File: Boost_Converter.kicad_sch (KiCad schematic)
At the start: 19 parts, among them U3 XL6019E1, U6 MCP4161-502E/SN

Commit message: inital layout
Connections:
- net Boost_In: no longer R18.2, R21.1, TP6.1, U6.5 (P0A)
- net GND: now also R18.2, R21.1, TP6.1, U6.5 (P0A)
- net SW_NODE: now reaches D2.2, L1.2, U3.3 (SW), U3.6 (SW)
- net Feeback: now reaches R14.2, R16.1, U3.5 (FB)
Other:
- moved on the sheet: R16, R21, R27, R28

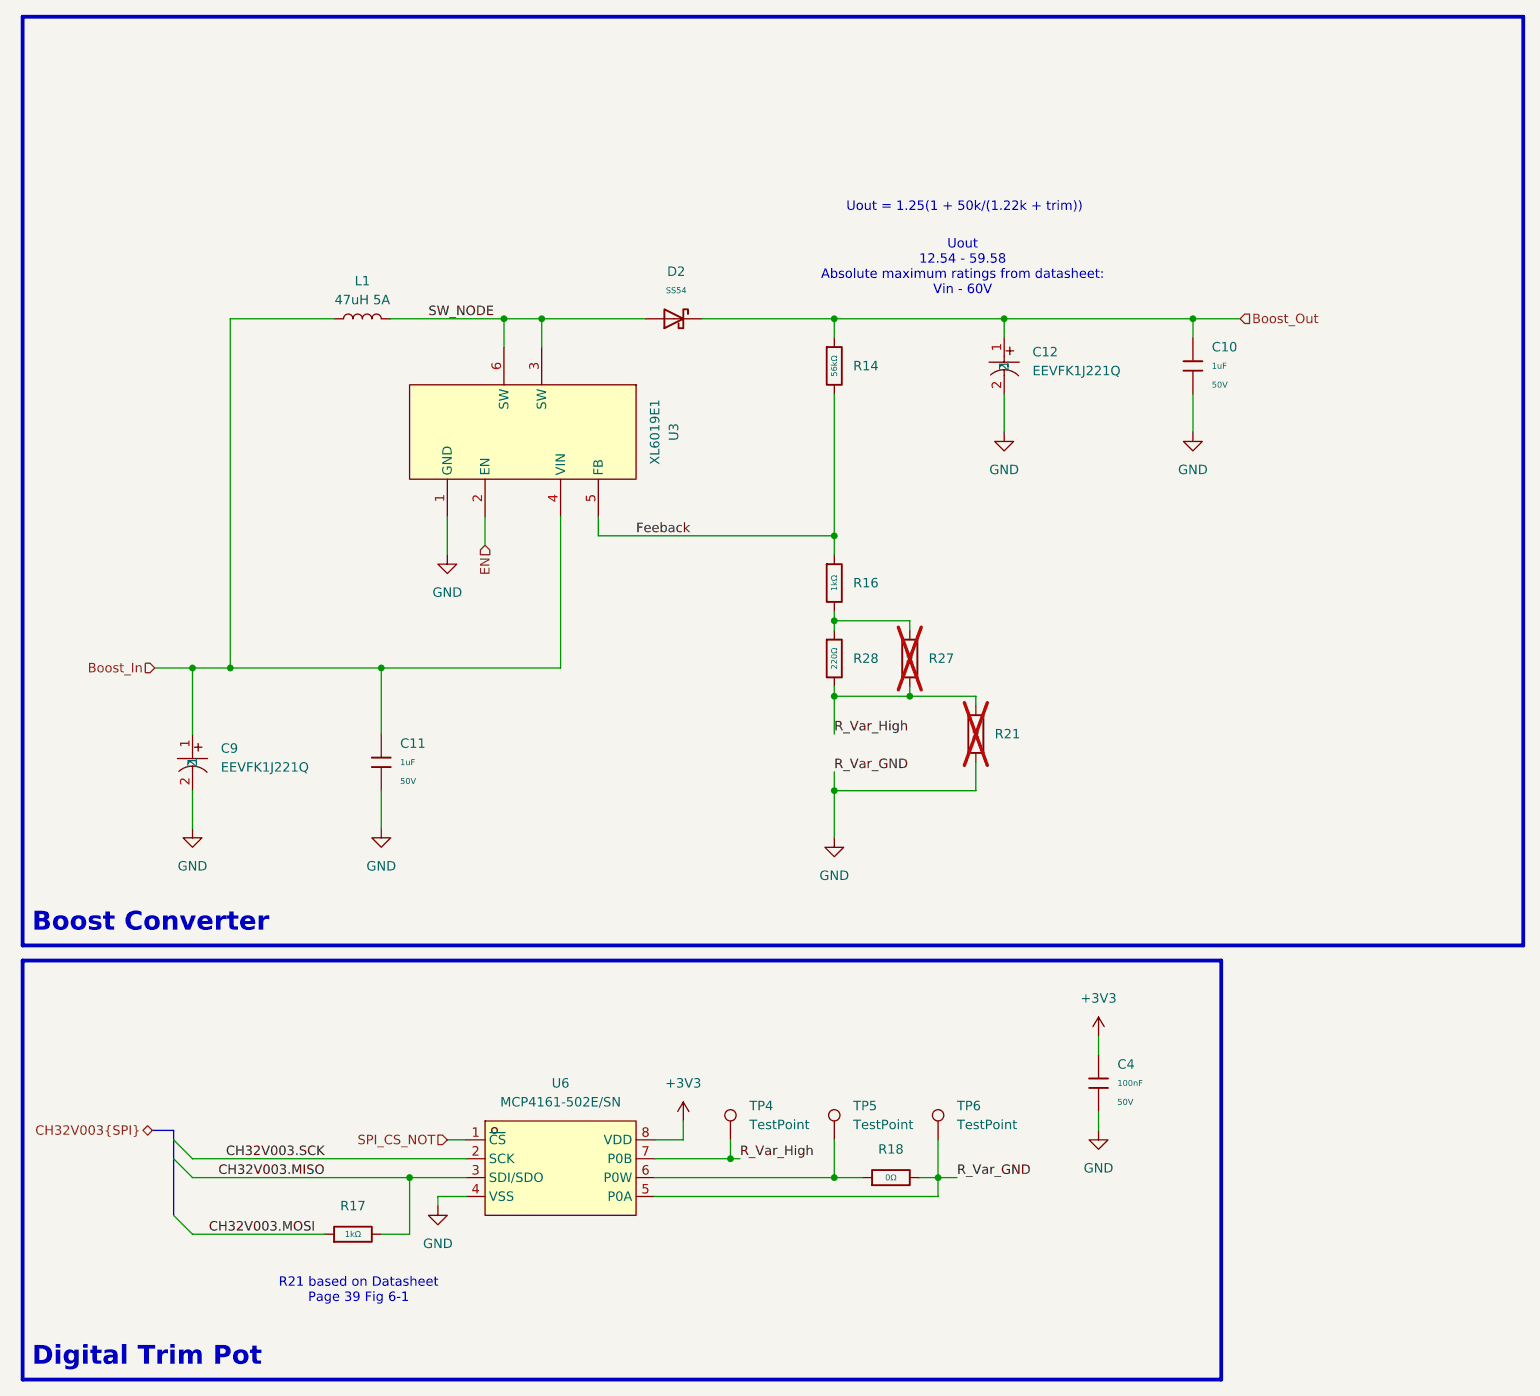
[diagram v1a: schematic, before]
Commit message: commit before removing all the diodes :"
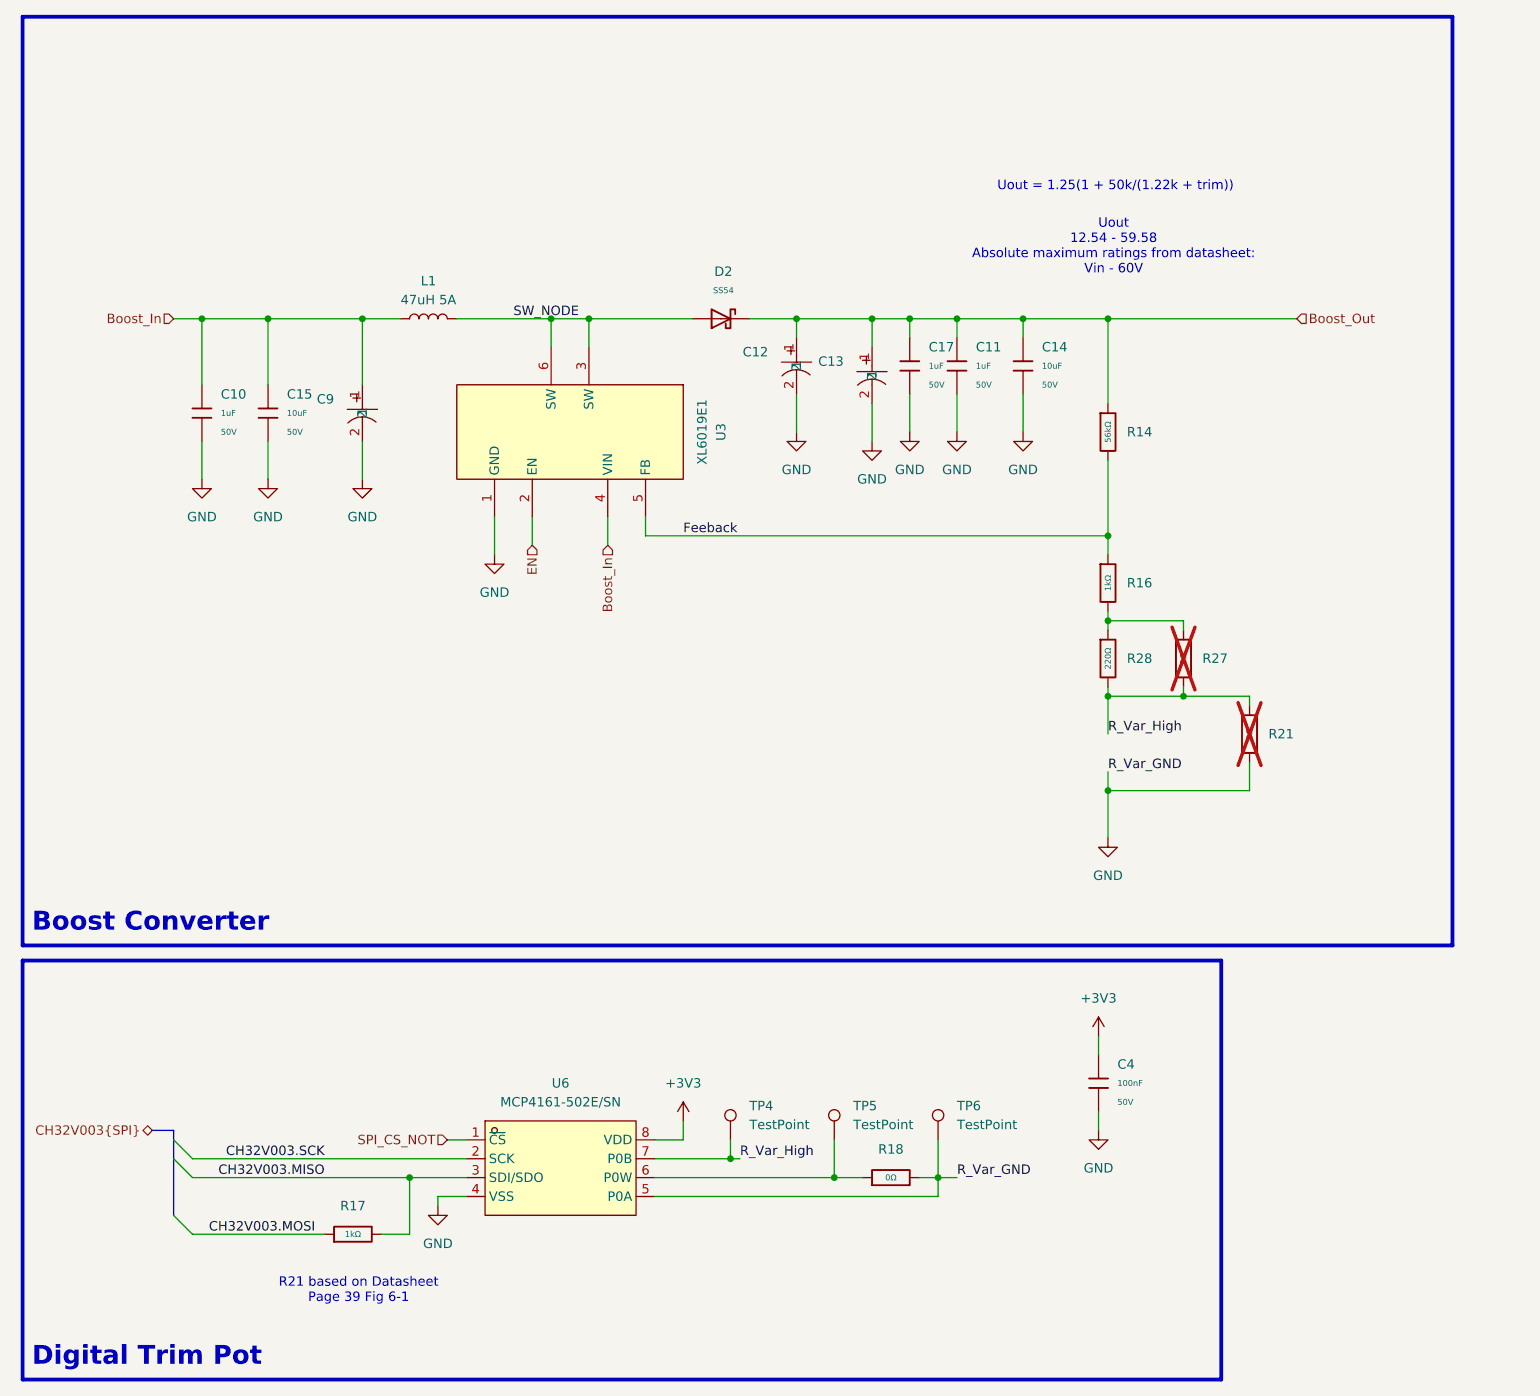
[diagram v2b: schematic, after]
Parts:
- added C13: Whatever the chinese man has (preferably 220uF), Capacitor_SMD:CP_Elec_10x10, symbol EEVFK1J221Q:EEVFK1J221Q
- added C14, C15: 10uF, PCM_JLCPCB:C_1206, symbol PCM_JLCPCB-Capacitors:1206,10uF
- added C17: 1uF, PCM_JLCPCB:C_0603, symbol PCM_JLCPCB-Capacitors:0603,1uF
- C12, C9: value EEVFK1J221Q -> Whatever the chinese man has (preferably 220uF); footprint EEVFK1J221Q:CAP-SMD_BD12.5-L13.5-W13.5-FD -> Capacitor_SMD:CP_Elec_10x10; KiLib_Generator (none) -> capacitor/SMD/elec_round_polarized
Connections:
- net Boost_In: now also C10.1, C15.1; no longer C11.1
- net Boost_Out: now also C11.1, C13.1, C14.1, C17.1; no longer C10.1
- net GND: now also C13.2, C14.2, C15.2, C17.2
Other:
- moved on the sheet: C9, D2, L1, U3
